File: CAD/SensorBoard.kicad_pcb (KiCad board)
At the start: 4 copper layers, 69.9 x 40 mm, 82 parts, among them J1 USB C 2.0, J2 SWD Connector, J3 UART Connector, J4 DAC Connector, M1 M1, M2 M2, M3 M3, M4 M4, SW1 SW_1, SW2 SW_2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

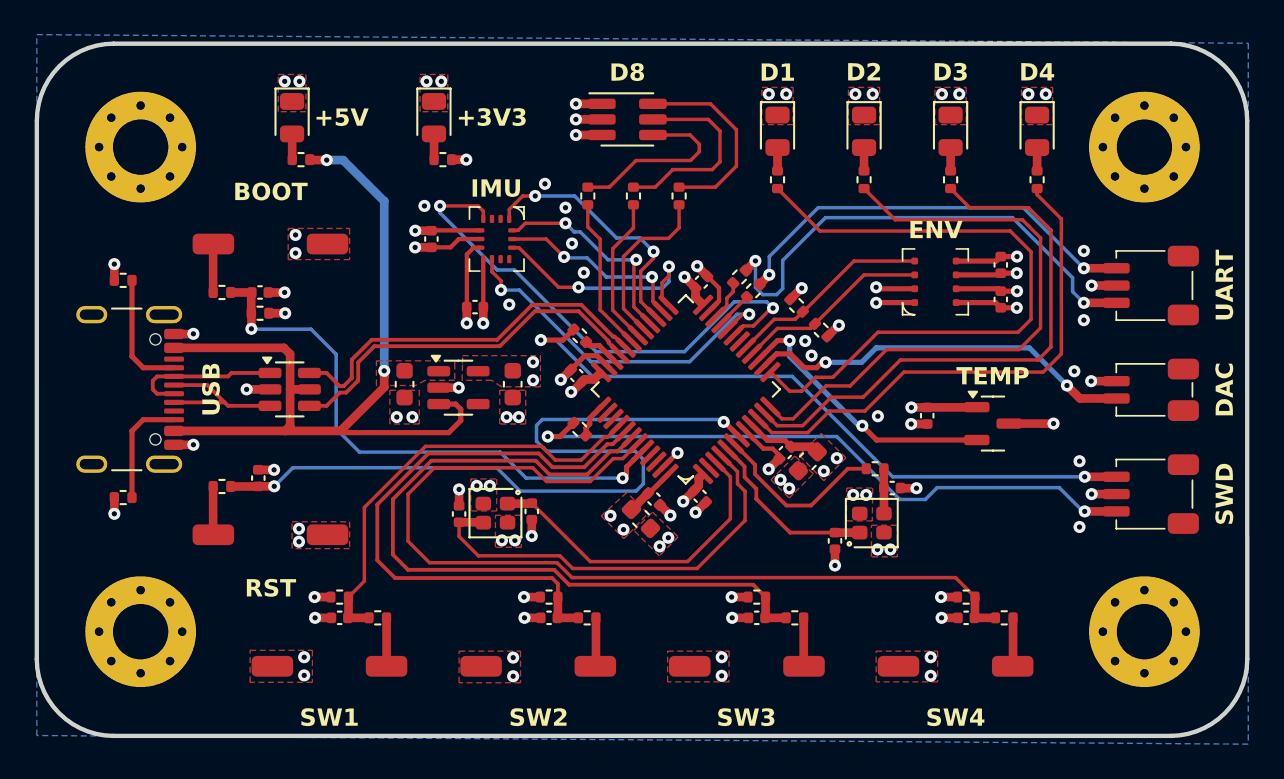
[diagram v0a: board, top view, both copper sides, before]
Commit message: Implement some feedback from Grig
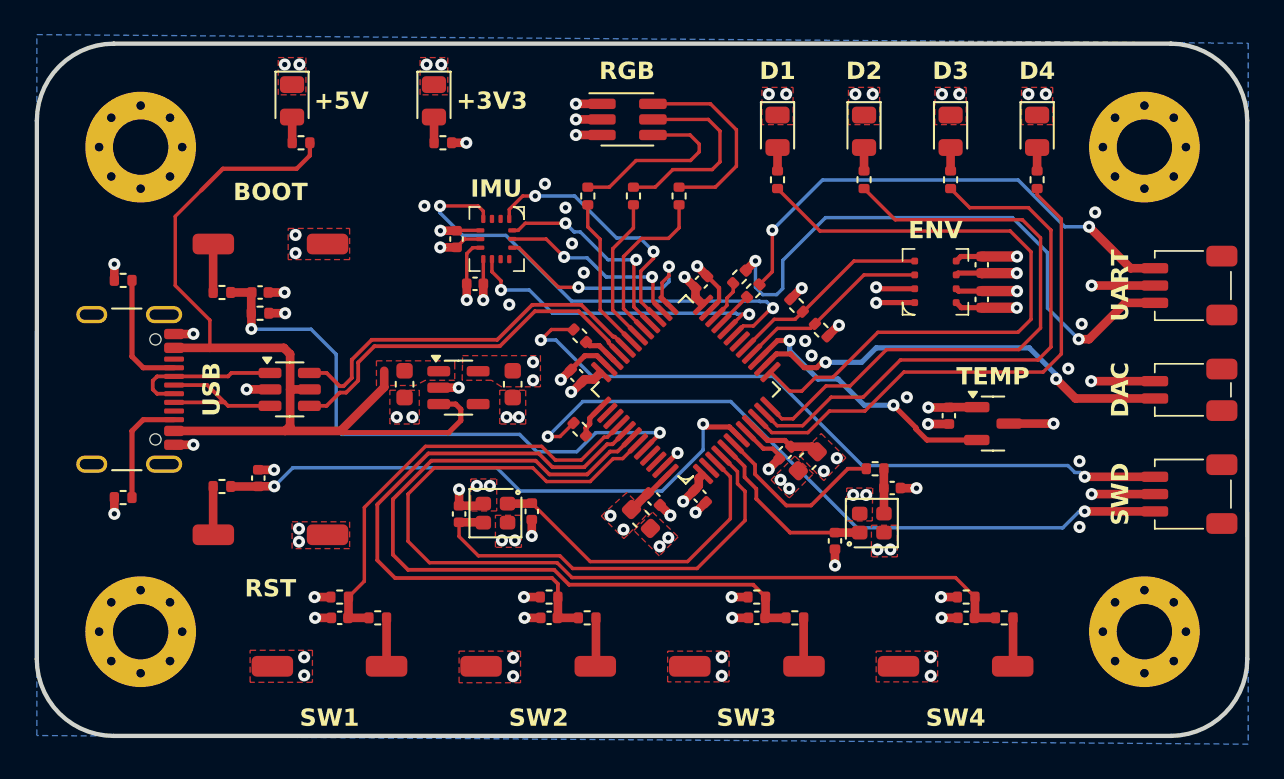
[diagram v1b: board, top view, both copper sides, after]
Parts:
- moved J2 2.22 mm to (189.1, 141.1)
- moved J3 2.22 mm to (189.1, 129.0)
- moved J4 2.22 mm to (189.1, 135.0)
- moved C24 1.45 mm to (146.8, 126.3)
- moved C23 1.34 mm to (147.8, 128.9)
- moved C22 1.25 mm to (175.2, 136.5)
- moved C20 1.10 mm to (177.1, 129.8)
- moved C21 1.10 mm to (177.1, 127.8)
- moved D6 0.97 mm to (137.2, 118.3)
- moved D7 0.97 mm to (145.4, 118.3)
- moved R10 0.97 mm to (146.0, 120.8)
- moved R9 0.97 mm to (137.8, 120.8)
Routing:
- net MCU_RST: track 46.3 -> 33.2 mm
- net GND: track 65.0 -> 70.4 mm
- net UART_RX: track 28.7 -> 34.0 mm
- net UART_TX: track 24.5 -> 28.9 mm
- net SWD_SWCLK: track 37.0 -> 41.1 mm
- net +3V3: track 36.9 -> 33.1 mm
- net +5V: track 51.5 -> 54.5 mm, vias 2 -> 0
- net IMU_INT1: track 30.3 -> 27.9 mm
- net DAC_OUT: track 22.6 -> 25.0 mm
- net IMU_INT2: track 20.8 -> 18.5 mm
- net SWD_SWDIO: track 38.7 -> 40.9 mm
- net MCU_BOOT: track 33.0 -> 34.2 mm
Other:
- board text added: "RGB"

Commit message: Update some placement of componenets and silkscreen
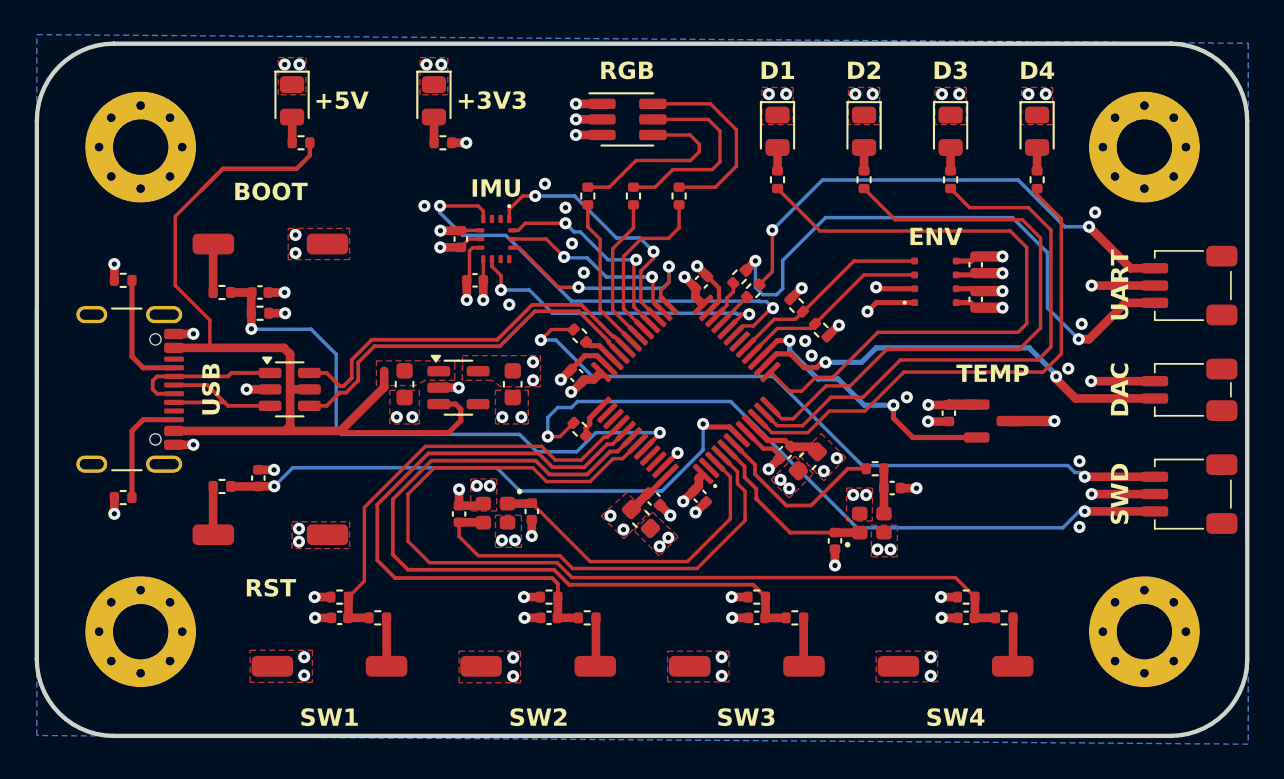
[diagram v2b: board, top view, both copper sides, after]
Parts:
- U6: footprint Package_TO_SOT_SMD:SOT-23 -> SensorBoard:SOT-23
- moved C20 0.35 mm to (176.8, 129.8)
- moved C21 0.35 mm to (176.8, 127.8)
- moved C24 0.25 mm to (147.0, 126.3)
- moved C23 0.20 mm to (147.8, 128.7)
- moved C22 0.15 mm to (175.2, 136.4)
- moved U6 0.14 mm to (177.8, 136.8)
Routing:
- net GND: track 70.4 -> 68.5 mm
- net +3V3: track 33.1 -> 31.1 mm
- net SWD_SWCLK: track 41.1 -> 41.8 mm
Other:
- outline, holes or cut-outs redrawn

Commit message: Add stitching vias and silkscreen icons
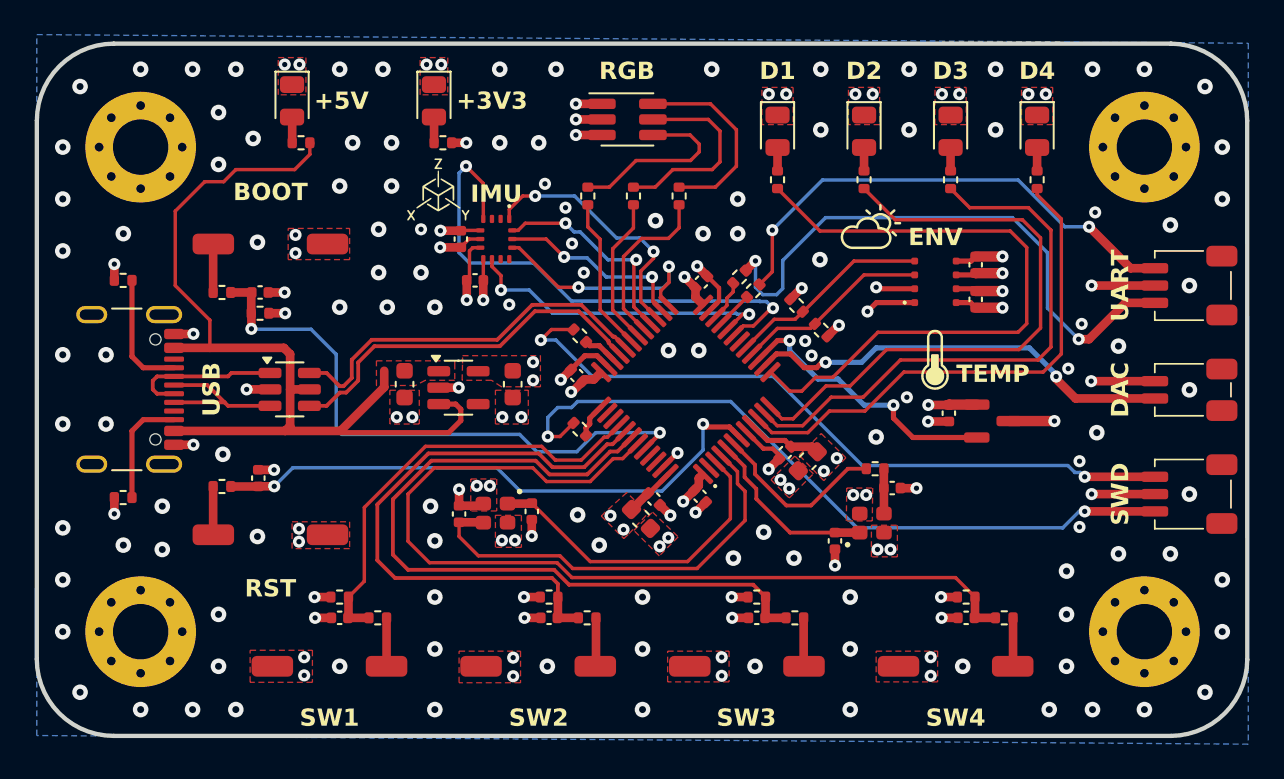
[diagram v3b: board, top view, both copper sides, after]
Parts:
- added G***: LOGO, LOGO, F.Cu at (170.7, 125.6)
- added G***: LOGO, LOGO, F.Cu at (145.7, 123.5)
- added G***: LOGO, LOGO, F.Cu at (174.4, 133.3)
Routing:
- net IMU_INT1: track 27.9 -> 31.0 mm
- net GND: vias 84 -> 187
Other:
- board text added: "SensorBoard Revision A Cristian Cristea"

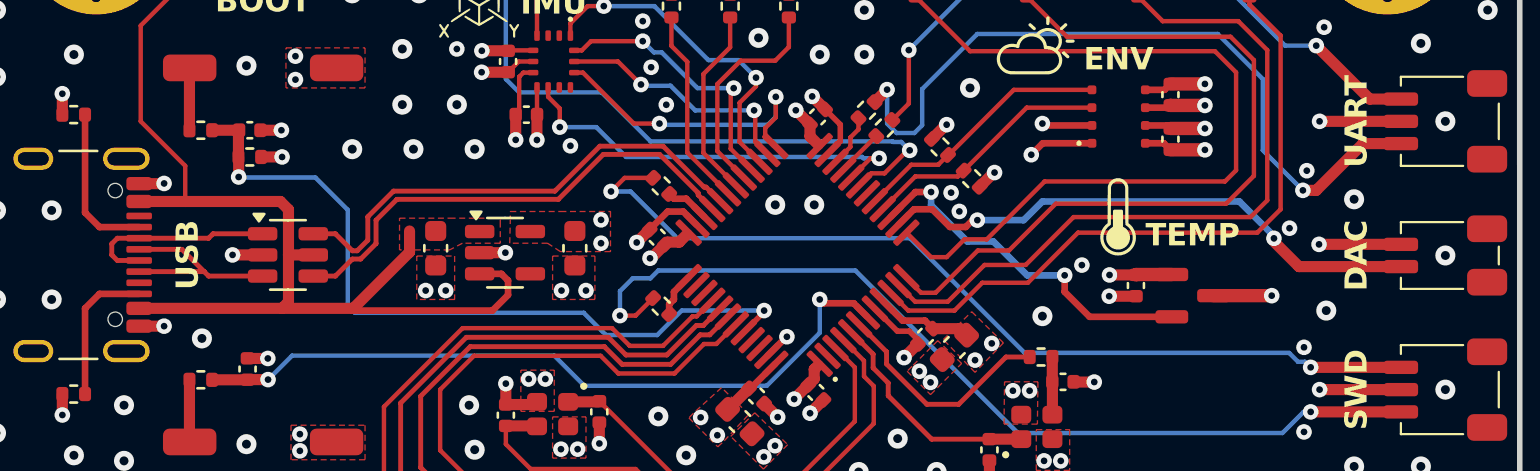
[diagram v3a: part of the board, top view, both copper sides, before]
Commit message: Update LDO
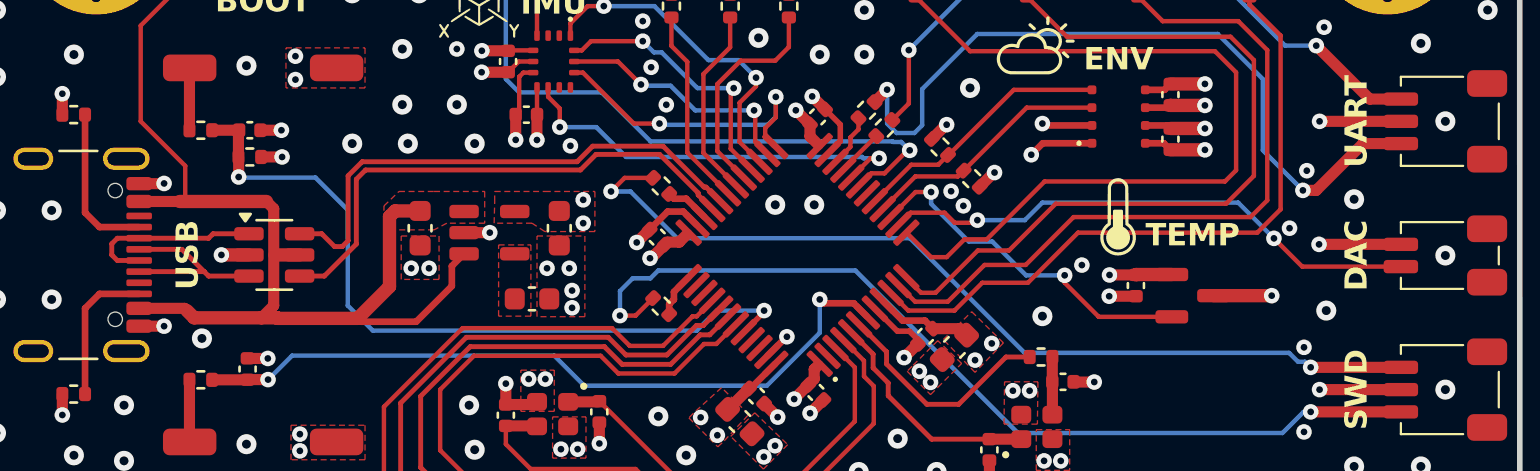
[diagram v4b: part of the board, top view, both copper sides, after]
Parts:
- added C25: 100n, Capacitor_SMD:C_0603_1608Metric, F.Cu at (148.1, 137.0)
- U2: value MIC5365 -> MIC5323-3.3YD5; footprint Package_TO_SOT_SMD:SOT-23-5 -> SensorBoard:SOT-23-5
- U6: footprint SensorBoard:SOT-23 -> SensorBoard:SOT-23-3
- moved U2 1.14 mm to (146.2, 134.0)
- moved C8 1.14 mm to (143.1, 133.8)
- moved C9 1.14 mm to (149.3, 133.8)
- moved U3 0.61 mm to (136.5, 135.0)
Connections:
- U2 pad 4: unconnected-(U2-NC-Pad4) -> /LDO_BYP
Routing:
- net USB_D+: track 21.9 -> 23.6 mm
- net USB_D-: track 22.2 -> 23.7 mm
- net /USB_CD-: track 8.79 -> 8.18 mm
- net /USB_CD+: track 8.96 -> 8.35 mm
- net GND: track 68.5 -> 68.4 mm, vias 187 -> 189
- added copper zone on F.Cu, net /LDO_BYP

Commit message: Update silkscreen
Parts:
- moved G*** 0.30 mm to (145.4, 123.4)
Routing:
- net +5V: track 54.3 -> 56.3 mm
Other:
- board text added: "TMP"
- board text removed: "TEMP"

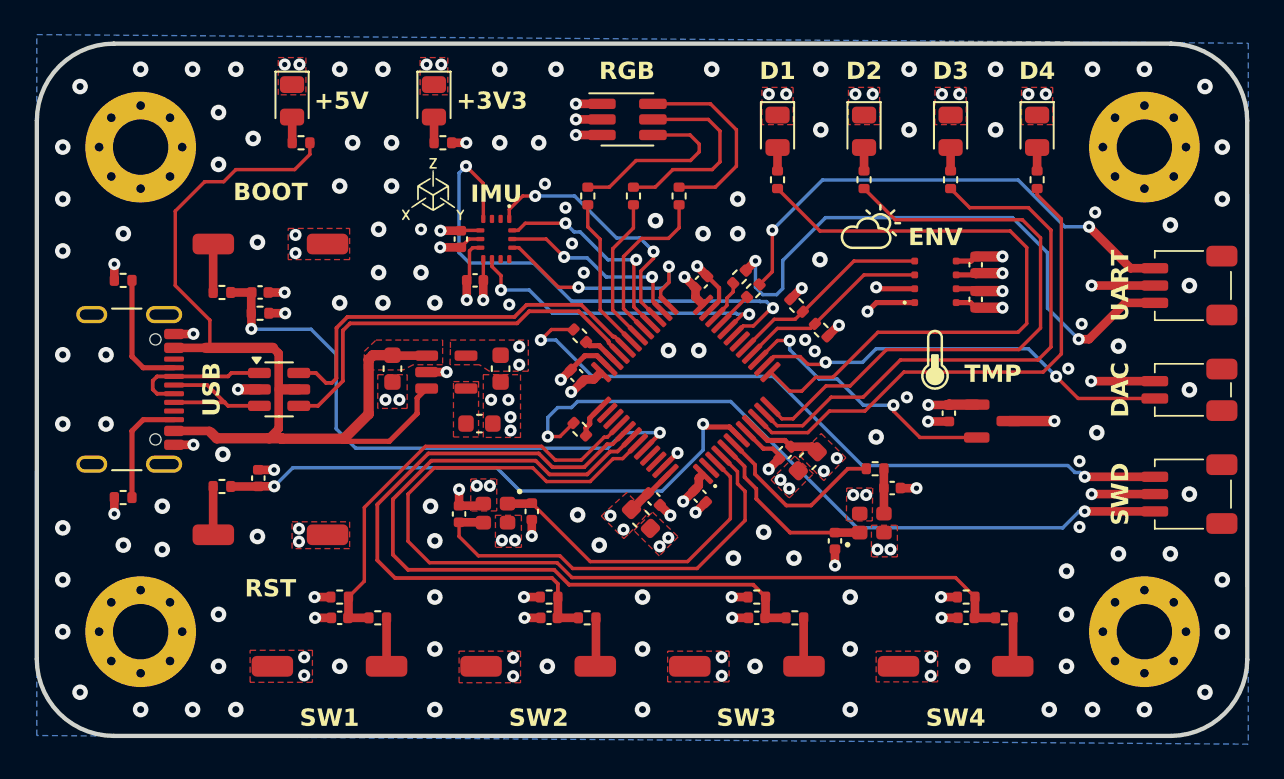
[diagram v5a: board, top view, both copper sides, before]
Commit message: Add keepout for crystals
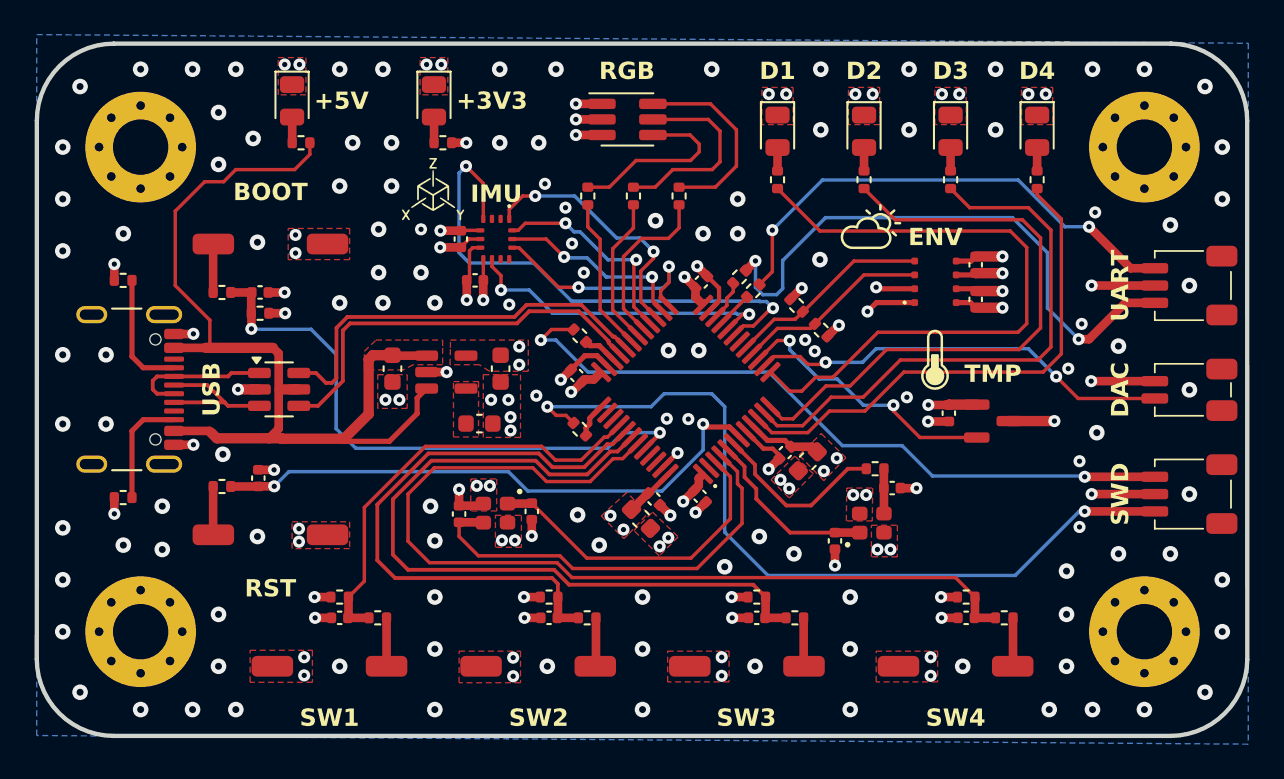
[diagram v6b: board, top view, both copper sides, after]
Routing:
- net SWD_SWCLK: track 41.8 -> 47.4 mm
- net GND: vias 189 -> 191

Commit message: Update silkscreen font
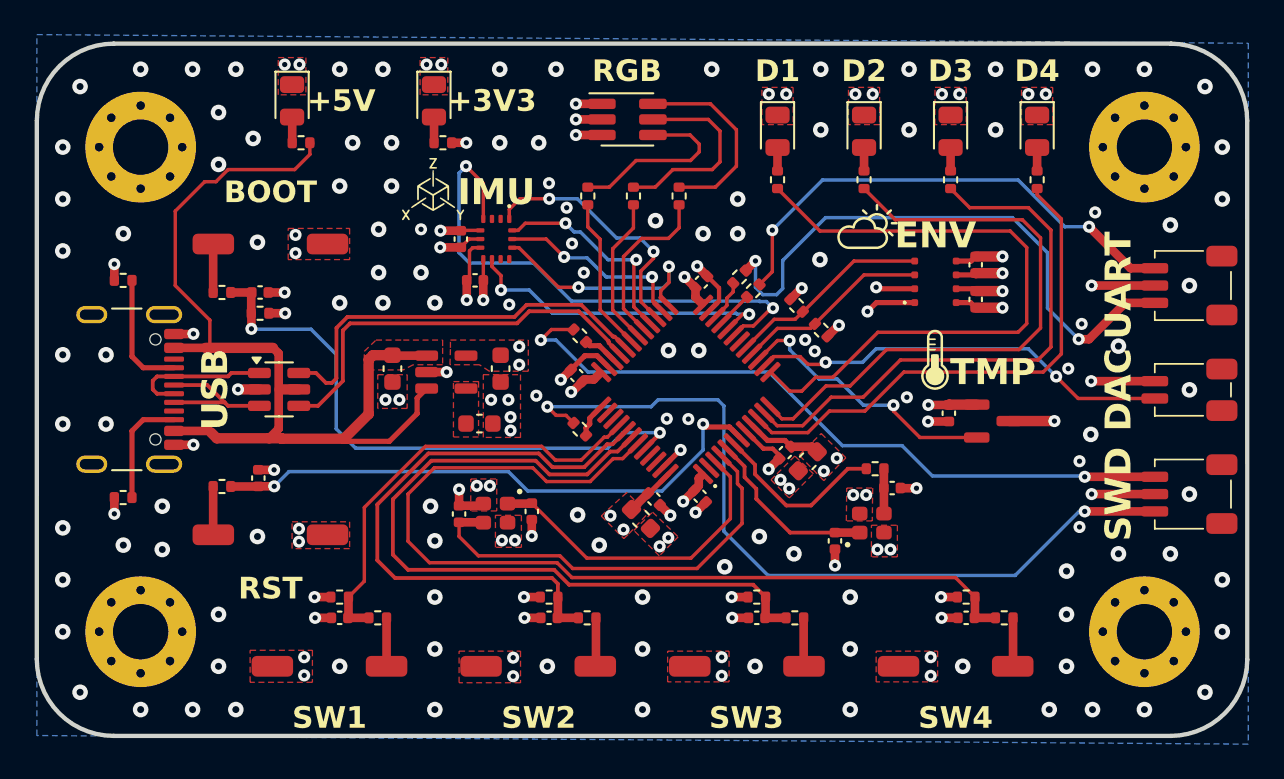
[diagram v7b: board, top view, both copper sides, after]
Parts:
- moved G*** 0.20 mm to (170.5, 125.6)
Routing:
- net GND: track 68.4 -> 68.6 mm, vias 191 -> 190
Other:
- board text added: "SensorBoard Revision A July 2024 Cristian Cristea"
- board text added: "github.com/cristiancristea00/SensorBoard"
- board text removed: "SensorBoard Revision A Cristian Cristea"
